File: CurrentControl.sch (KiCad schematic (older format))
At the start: 7 parts, among them P1 HEATSINK, Q401 BUK9575, U201 LMV358

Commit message: updated schematic capacitor symbols to use new default library symbols
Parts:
- R401, R402, R403: symbol R -> R-RESCUE-CurrentSinkOrSwim
- RV401: symbol POT -> POT-RESCUE-CurrentSinkOrSwim
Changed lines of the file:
@@
 EESchema Schematic File Version 2
+LIBS:CurrentSinkOrSwim-rescue
 LIBS:power
 LIBS:device
@@
 LIBS:memory
 LIBS:xilinx
-LIBS:special
 LIBS:microcontrollers
 LIBS:dsp
@@
 $EndComp
 $Comp
-L R R403
+L R-RESCUE-CurrentSinkOrSwim R403
 U 1 1 54DADC66
 P 8100 5150
@@
 Connection ~ 8100 5450
 $Comp
-L POT RV401
+L POT-RESCUE-CurrentSinkOrSwim RV401
 U 1 1 54DADC9B
 P 3750 4050
@@
 	8650 1500 8100 1500
 $Comp
-L R R402
+L R-RESCUE-CurrentSinkOrSwim R402
 U 1 1 54DAE31B
 P 6450 3700
@@
 $EndComp
 $Comp
-L R R401
+L R-RESCUE-CurrentSinkOrSwim R401
 U 1 1 54DADC7B
 P 3750 3100

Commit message: updated diode to sod-323 package and used new schematic symbol because pin numbers changed
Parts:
- R403: footprint Resistors_ThroughHole:Resistor_Horizontal_RM15mm -> Resistors_SMD:R_1206; Fieldname (none) -> Alt TH Part: AC01000001007JA100; MPN AC01000001007JA100 -> RUW3216FR100CS
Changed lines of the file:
@@
 F 0 "R403" V 8180 5150 50  0000 C CNN
 F 1 ".1" V 8107 5151 50  0000 C CNN
-F 2 "Resistors_ThroughHole:Resistor_Horizontal_RM15mm" V 8030 5150 30  0001 C CNN
+F 2 "Resistors_SMD:R_1206" V 8030 5150 30  0001 C CNN
 F 3 "" H 8100 5150 30  0000 C CNN
-F 4 "AC01000001007JA100" V 8100 5150 60  0001 C CNN "MPN"
+F 4 "Alt TH Part: AC01000001007JA100" H 8100 5150 60  0001 C CNN "Fieldname"
+F 5 "RUW3216FR100CS" V 8100 5150 60  0001 C CNN "MPN"
 	1    8100 5150
 	1    0    0    -1

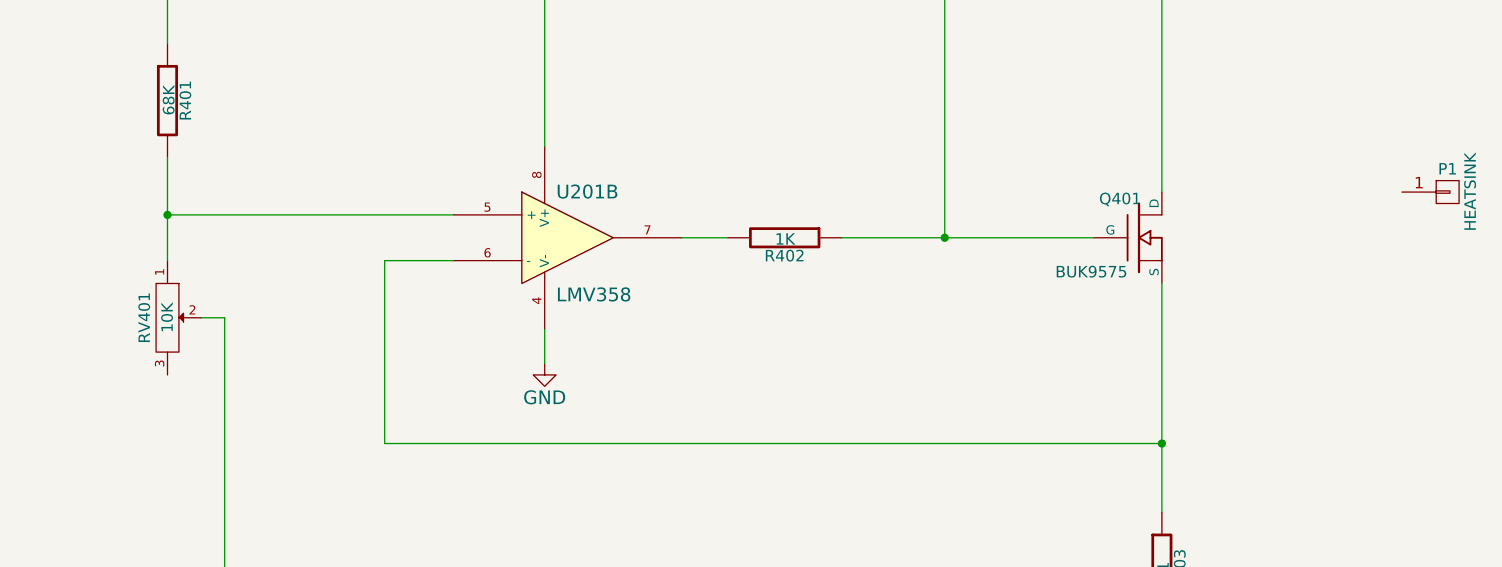
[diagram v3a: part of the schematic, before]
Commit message: added 100uF pcb footprint and misc comments
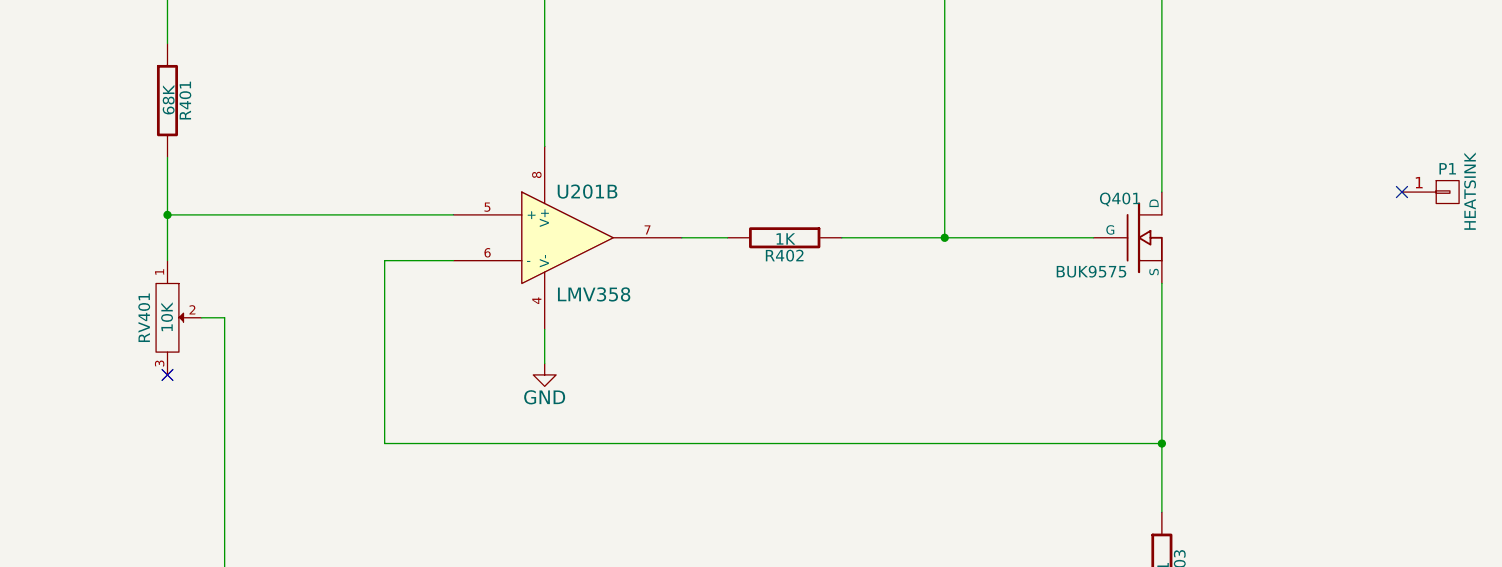
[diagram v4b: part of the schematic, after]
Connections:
- no-connect marks 0 -> 2
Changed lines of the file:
@@
 Wire Wire Line
 	4000 5450 8100 5450
+NoConn ~ 3750 4300
+NoConn ~ 9150 3500
 $EndSCHEMATC

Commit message: initial component placement on the pcb
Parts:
- Q401: footprint Transistors_TO-220:TO-220_FET-GDS_Vertical -> Current:TO-220_FET-GDS_Vertical
- R401, R402: footprint SMD_Packages:SMD-0805 -> Resistors_SMD:R_0805
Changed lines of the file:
@@
 F 0 "Q401" H 8010 3870 50  0000 R CNN
 F 1 "BUK9575" H 7950 3550 50  0000 R CNN
-F 2 "Transistors_TO-220:TO-220_FET-GDS_Vertical" H 8000 3700 60  0001 C CNN
+F 2 "Current:TO-220_FET-GDS_Vertical" H 8000 3700 60  0001 C CNN
 F 3 "" H 8000 3700 60  0000 C CNN
 F 4 "BUK9575-100A,127" H 8000 3700 60  0001 C CNN "MPN"
@@
 F 0 "R402" V 6530 3700 50  0000 C CNN
 F 1 "1K" V 6457 3701 50  0000 C CNN
-F 2 "SMD_Packages:SMD-0805" V 6380 3700 30  0001 C CNN
+F 2 "Resistors_SMD:R_0805" V 6380 3700 30  0001 C CNN
 F 3 "" H 6450 3700 30  0000 C CNN
 	1    6450 3700
@@
 F 0 "R401" V 3830 3100 50  0000 C CNN
 F 1 "68K" V 3757 3101 50  0000 C CNN
-F 2 "SMD_Packages:SMD-0805" V 3680 3100 30  0001 C CNN
+F 2 "Resistors_SMD:R_0805" V 3680 3100 30  0001 C CNN
 F 3 "" H 3750 3100 30  0000 C CNN
 	1    3750 3100

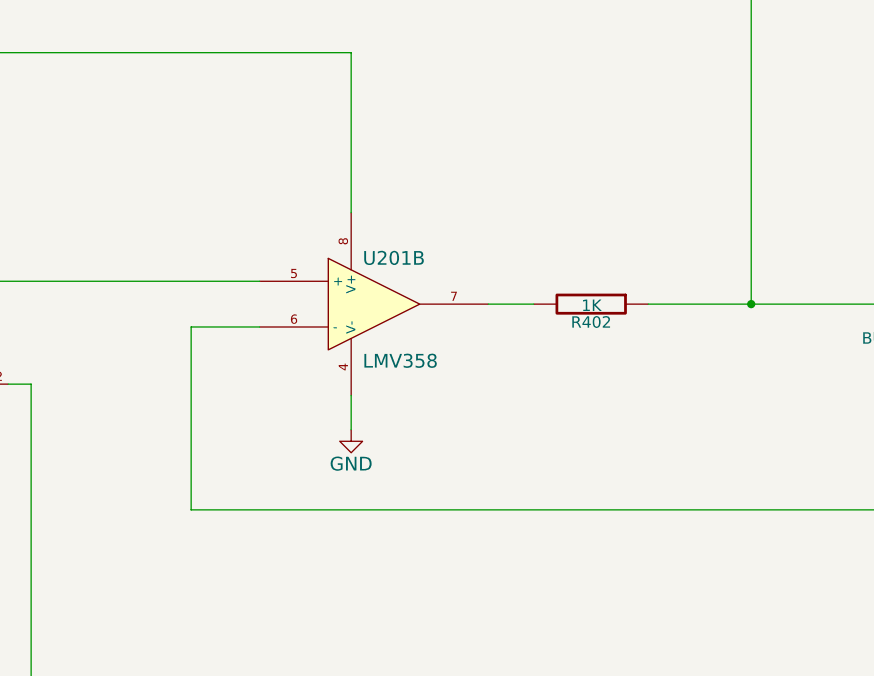
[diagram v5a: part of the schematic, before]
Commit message: added test points to  schematic and pcb
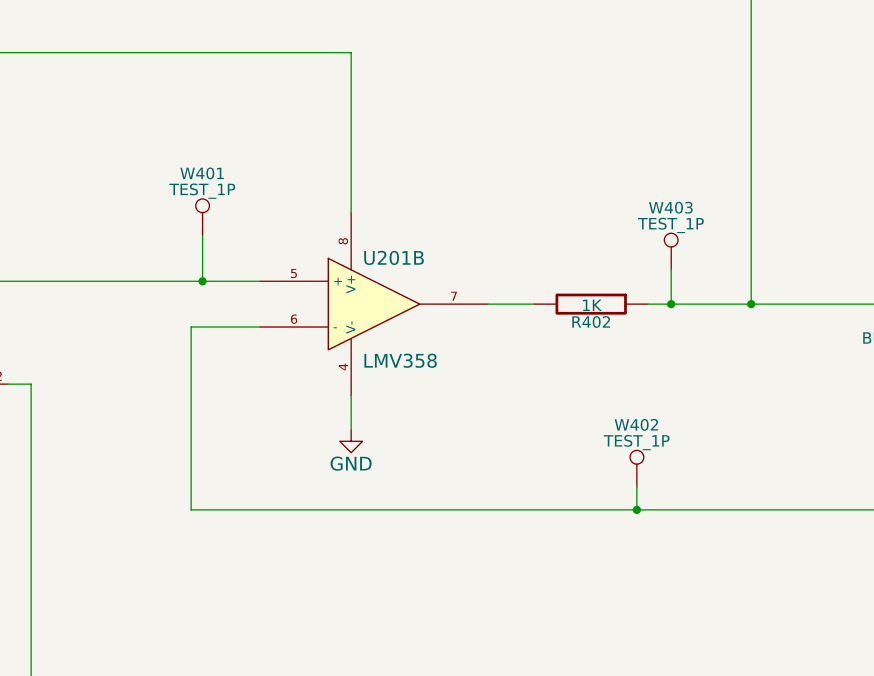
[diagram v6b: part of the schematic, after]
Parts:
- added W401, W402, W403: TEST_1P, Measurement_Points:Measurement_Point_Round-SMD-Pad_Small, symbol TEST_1P
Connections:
- net FET_Gate: now also W403.1
- net at R401.2, RV401.1, U201.5 (+): now also W401.1
- net at Q401.S, R403.1, U201.6 (-): now also W402.1
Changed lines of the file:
@@
 NoConn ~ 3750 4300
 NoConn ~ 9150 3500
+$Comp
+L TEST_1P W402
+U 1 1 57C8579B
+P 6650 4500
+F 0 "W402" H 6650 4770 50  0000 C CNN
+F 1 "TEST_1P" H 6650 4700 50  0000 C CNN
+F 2 "Measurement_Points:Measurement_Point_Round-SMD-Pad_Small" H 6850 4500 50  0001 C CNN
+F 3 "" H 6850 4500 50  0000 C CNN
+	1    6650 4500
+	1    0    0    -1
+$EndComp
+Wire Wire Line
+	6650 4500 6650 4600
+Connection ~ 6650 4600
+$Comp
+L TEST_1P W403
+U 1 1 57C85818
+P 6800 3550
+F 0 "W403" H 6800 3820 50  0000 C CNN
+F 1 "TEST_1P" H 6800 3750 50  0000 C CNN
+F 2 "Measurement_Points:Measurement_Point_Round-SMD-Pad_Small" H 7000 3550 50  0001 C CNN
+F 3 "" H 7000 3550 50  0000 C CNN
+	1    6800 3550
+	1    0    0    -1
+$EndComp
+$Comp
+L TEST_1P W401
+U 1 1 57C85856
+P 4750 3400
+F 0 "W401" H 4750 3670 50  0000 C CNN
+F 1 "TEST_1P" H 4750 3600 50  0000 C CNN
+F 2 "Measurement_Points:Measurement_Point_Round-SMD-Pad_Small" H 4950 3400 50  0001 C CNN
+F 3 "" H 4950 3400 50  0000 C CNN
+	1    4750 3400
+	1    0    0    -1
+$EndComp
+Wire Wire Line
+	4750 3400 4750 3600
+Connection ~ 4750 3600
+Wire Wire Line
+	6800 3550 6800 3700
+Connection ~ 6800 3700
 $EndSCHEMATC

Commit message: changed sense resistor to 2W, 2512SMD2
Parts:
- R403: footprint Resistors_SMD:R_1206 -> Resistors_SMD:R_2512; MPN RUW3216FR100CS -> CRA2512-FZ-R100ELF
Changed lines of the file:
@@
 F 0 "R403" V 8180 5150 50  0000 C CNN
 F 1 ".1" V 8107 5151 50  0000 C CNN
-F 2 "Resistors_SMD:R_1206" V 8030 5150 30  0001 C CNN
+F 2 "Resistors_SMD:R_2512" V 8030 5150 30  0001 C CNN
 F 3 "" H 8100 5150 30  0000 C CNN
 F 4 "Alt TH Part: AC01000001007JA100" H 8100 5150 60  0001 C CNN "Fieldname"
-F 5 "RUW3216FR100CS" V 8100 5150 60  0001 C CNN "MPN"
+F 5 "CRA2512-FZ-R100ELF" V 8100 5150 60  0001 C CNN "MPN"
 	1    8100 5150
 	1    0    0    -1
